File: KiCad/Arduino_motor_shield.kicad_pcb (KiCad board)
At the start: 2 copper layers, 25.9 x 59.9 mm, 19 parts, among them J1 Arduino header 1, J2 DC jack, J3 Arduino header 2, J4 Motors conn, U1 TB6612FNG

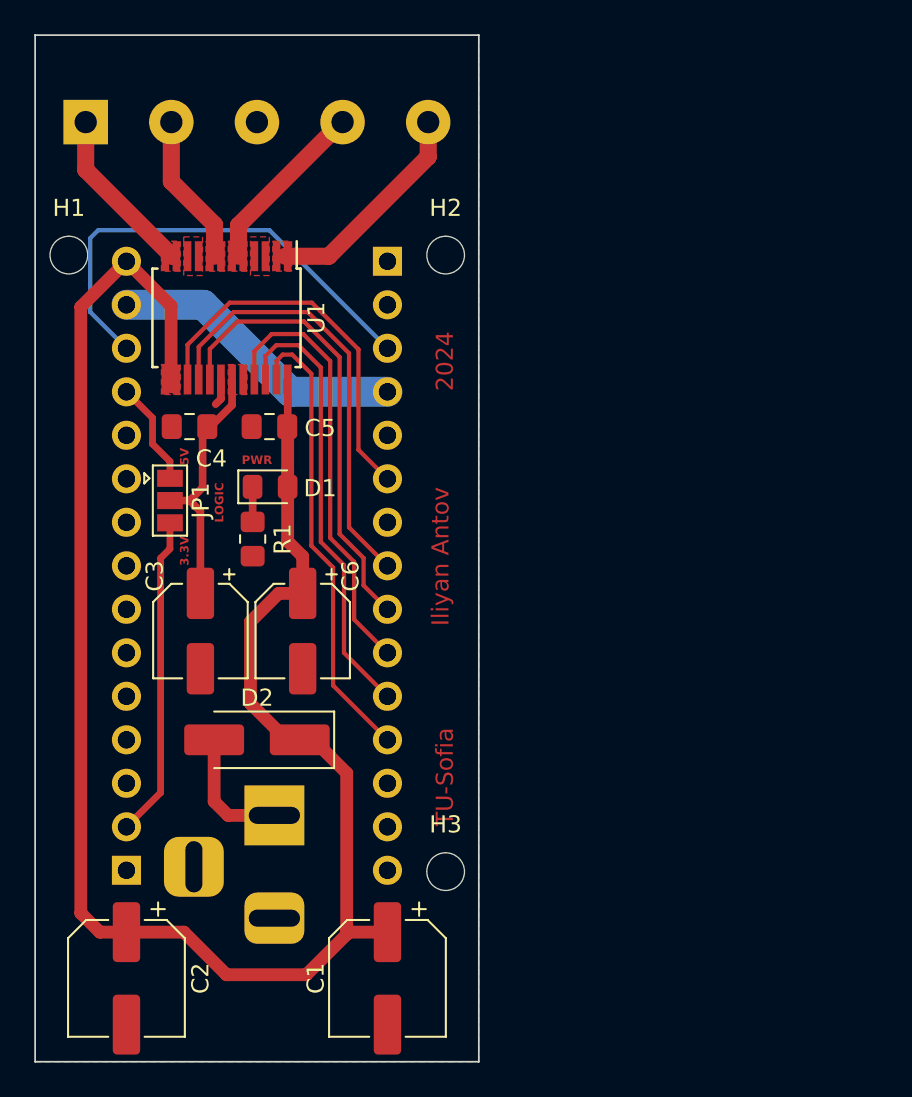
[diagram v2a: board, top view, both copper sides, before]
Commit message: Freed up a PWM pin on the Arduino
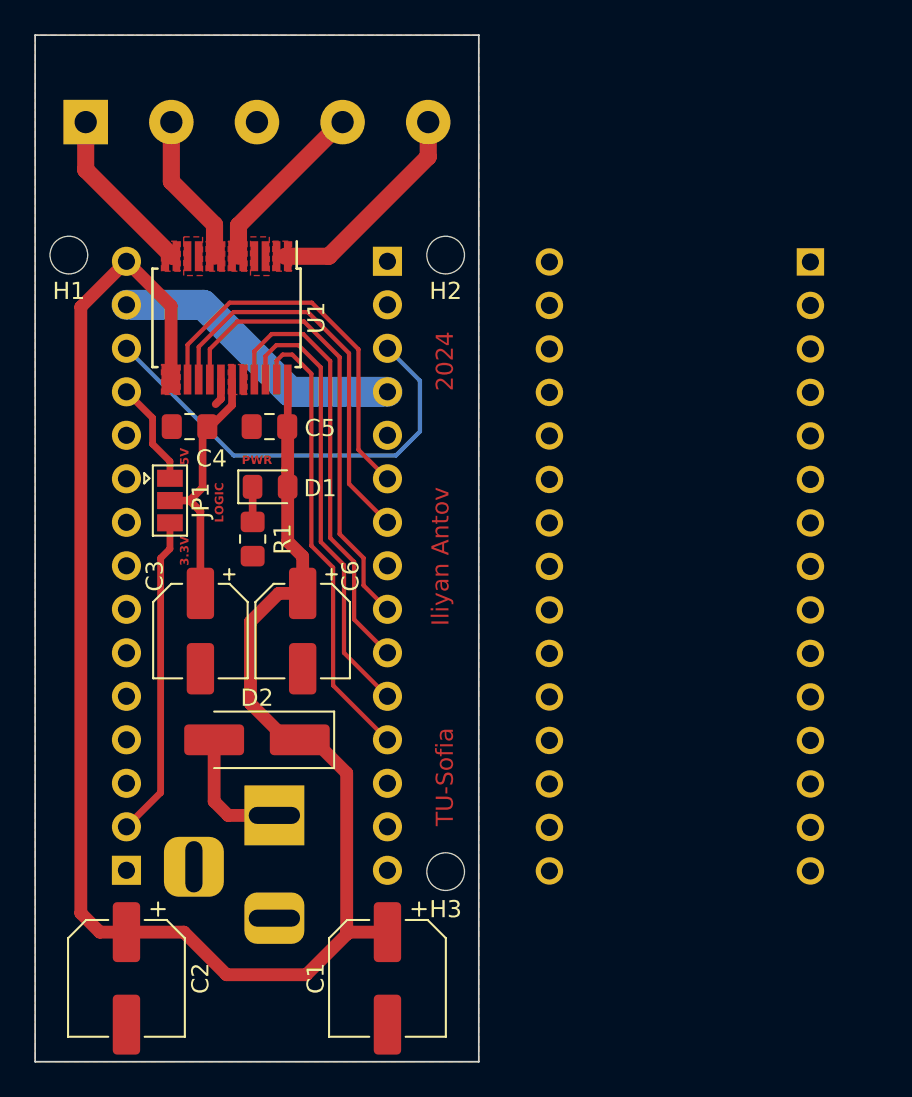
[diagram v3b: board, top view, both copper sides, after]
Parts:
- moved A1 24.7 mm to (166.3, 77.8)
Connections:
- U1 pad 16: /~D5 -> /D4
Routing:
- net /~D5: track 25.9 -> 0.00 mm
- net /D4: track 0.00 -> 23.3 mm
- net /~{RESET}: track 27.7 -> 25.9 mm
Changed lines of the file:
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@@
     (property "ki_keywords" "mounting hole")
     (attr exclude_from_pos_files)
-    (fp_text reference "H3" (at 0 -2.75) (layer "F.SilkS")
+    (fp_text reference "H3" (at 0 2.2) (layer "F.SilkS")
         (effects (font (size 1 1) (thickness 0.15)))
     )
@@
       (net 42 "/~D3") (pinfunction "PWMB") (pintype "input"))
     (pad "16" smd rect (at 3.6 1.625 270) (size 1.75 0.45) (layers "F.Cu" "F.Paste" "F.Mask")
-      (net 37 "/~D5") (pinfunction "BIN2") (pintype "input"))
+      (net 43 "/D4") (pinfunction "BIN2") (pintype "input"))
     (pad "17" smd rect (at 3.6 0.975 270) (size 1.75 0.45) (layers "F.Cu" "F.Paste" "F.Mask")
       (net 36 "/~D6") (pinfunction "BIN1") (pintype "input"))
@@
     (property "ki_keywords" "mounting hole")
     (attr exclude_from_pos_files)
-    (fp_text reference "H1" (at 0 -2.75) (layer "F.SilkS")
+    (fp_text reference "H1" (at 0 2.1) (layer "F.SilkS")
         (effects (font (size 1 1) (thickness 0.15)))
     )
@@
     (property "ki_keywords" "mounting hole")
     (attr exclude_from_pos_files)
-    (fp_text reference "H2" (at 0 -2.75) (layer "F.SilkS")
+    (fp_text reference "H2" (at 0 2.1) (layer "F.SilkS")
         (effects (font (size 1 1) (thickness 0.15)))
     )
@@
   )
   (footprint "Module:Arduino_Nano" (layer "B.Cu")
-    (at 141.60276 77.764 180)
+    (at 166.3 77.8 180)
     (descr "Arduino Nano, http://www.mouser.com/pdfdocs/Gravitech_Arduino_Nano3_0.pdf")
     (tags "Arduino Nano")
@@
   (segment (start 136.728294 81.28) (end 132.842 81.28) (width 0.25) (layer "F.Cu") (net 36))
   (segment (start 131.22976 82.89224) (end 131.22976 84.666) (width 0.25) (layer "F.Cu") (net 36))
-  (segment (start 132.614183 80.73) (end 136.956112 80.73) (width 0.25) (layer "F.Cu") (net 37))
-  (segment (start 130.57976 84.666) (end 130.57976 82.764423) (width 0.25) (layer "F.Cu") (net 37))
-  (segment (start 136.956112 80.73) (end 139.36 83.133888) (width 0.25) (layer "F.Cu") (net 37))
-  (segment (start 130.57976 82.764423) (end 132.614183 80.73) (width 0.25) (layer "F.Cu") (net 37))
-  (segment (start 139.36 93.30124) (end 141.60276 95.544) (width 0.25) (layer "F.Cu") (net 37))
-  (segment (start 139.36 83.133888) (end 139.36 93.30124) (width 0.25) (layer "F.Cu") (net 37))
   (segment (start 135.001 110.118) (end 132.30076 110.118) (width 0.75) (layer "F.Cu") (net 38))
   (segment (start 131.48276 109.3) (end 131.48276 105.704) (width 0.75) (layer "F.Cu") (net 38))
   (segment (start 132.30076 110.118) (end 131.48276 109.3) (width 0.75) (layer "F.Cu") (net 38))
-  (segment (start 134.70476 75.946) (end 141.60276 82.844) (width 0.25) (layer "B.Cu") (net 40))
-  (segment (start 126.36276 82.844) (end 124.25 80.73124) (width 0.25) (layer "B.Cu") (net 40))
-  (segment (start 124.714 75.946) (end 134.70476 75.946) (width 0.25) (layer "B.Cu") (net 40))
-  (segment (start 124.25 76.41) (end 124.714 75.946) (width 0.25) (layer "B.Cu") (net 40))
-  (segment (start 124.25 80.73124) (end 124.25 76.41) (width 0.25) (layer "B.Cu") (net 40))
+  (segment (start 126.36276 82.844) (end 132.61776 89.099) (width 0.25) (layer "B.Cu") (net 40))
+  (segment (start 132.61776 89.099) (end 142.101 89.099) (width 0.25) (layer "B.Cu") (net 40))
+  (segment (start 142.101 89.099) (end 143.5 87.7) (width 0.25) (layer "B.Cu") (net 40))
+  (segment (start 143.5 84.74124) (end 141.60276 82.844) (width 0.25) (layer "B.Cu") (net 40))
+  (segment (start 143.5 87.7) (end 143.5 84.74124) (width 0.25) (layer "B.Cu") (net 40))
   (segment (start 137.18393 80.18) (end 132.386365 80.18) (width 0.25) (layer "F.Cu") (net 42))
   (segment (start 141.60276 90.464) (end 139.91 88.77124) (width 0.25) (layer "F.Cu") (net 42))
@@
   (segment (start 139.91 88.77124) (end 139.91 82.90607) (width 0.25) (layer "F.Cu") (net 42))
   (segment (start 132.386365 80.18) (end 129.92976 82.636605) (width 0.25) (layer "F.Cu") (net 42))
+  (segment (start 130.57976 82.764423) (end 132.614183 80.73) (width 0.25) (layer "F.Cu") (net 43))
+  (segment (start 132.614183 80.73) (end 136.956112 80.73) (width 0.25) (layer "F.Cu") (net 43))
+  (segment (start 139.36 90.76124) (end 141.60276 93.004) (width 0.25) (layer "F.Cu") (net 43))
+  (segment (start 136.956112 80.73) (end 139.36 83.133888) (width 0.25) (layer "F.Cu") (net 43))
+  (segment (start 130.57976 84.666) (end 130.57976 82.764423) (width 0.25) (layer "F.Cu") (net 43))
+  (segment (start 139.36 83.133888) (end 139.36 90.76124) (width 0.25) (layer "F.Cu") (net 43))
   (segment (start 139.658 98.67924) (end 139.658 95.314993) (width 0.25) (layer "F.Cu") (net 44))
   (segment (start 134.843524 82.012) (end 133.82976 83.025764) (width 0.25) (layer "F.Cu") (net 44))
@@
       )
     )
-  )
-  (zone (net 0) (net_name "") (layer "F.Mask") (hatch edge 0.5)
-    (connect_pads (clearance 0.25))
-    (min_thickness 0.25) (filled_areas_thickness no)
-    (fill yes (thermal_gap 0.5) (thermal_bridge_width 0.5))
-    (polygon
-      (pts
-        (xy 121 64.5)
-        (xy 147 64.5)
-        (xy 147 124.5)
-        (xy 121 124.5)
-      )
-    )

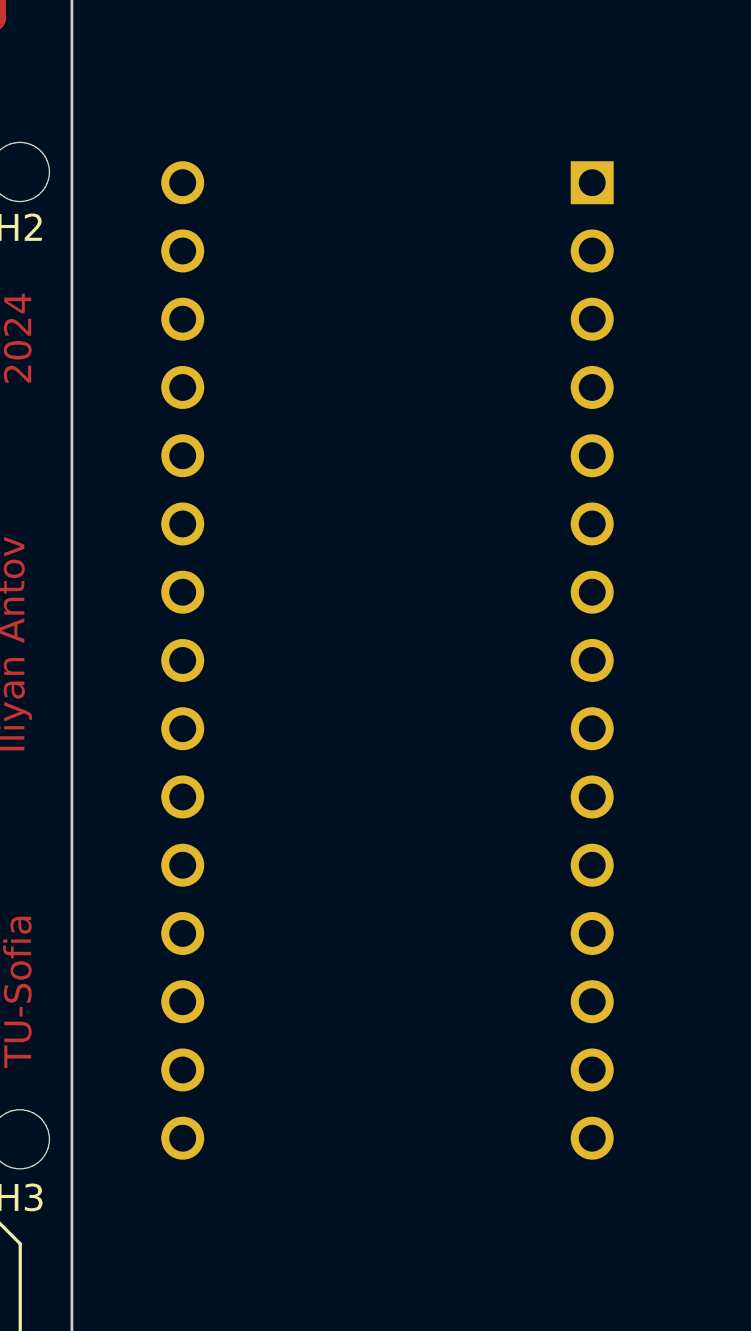
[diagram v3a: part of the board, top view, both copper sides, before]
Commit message: Added manufacture data PDF
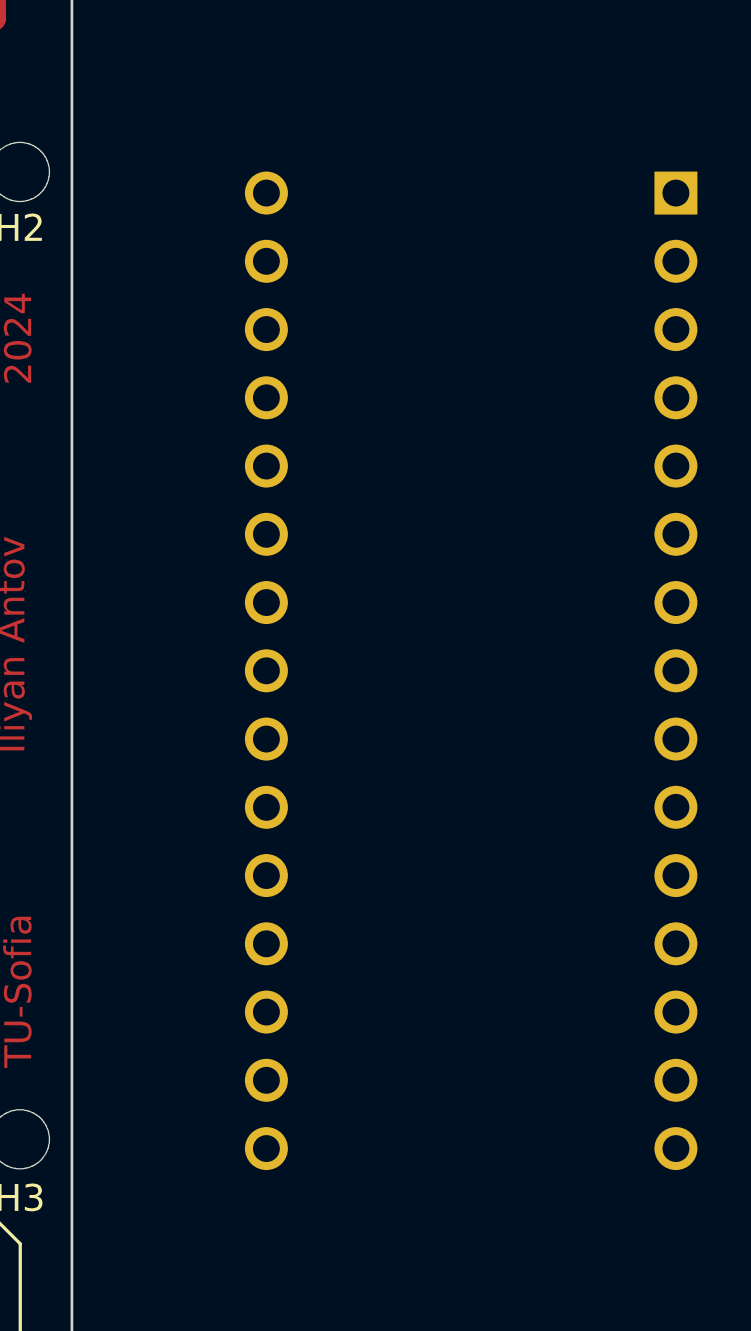
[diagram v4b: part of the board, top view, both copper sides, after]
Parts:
- moved A1 3.14 mm to (169.4, 78.2)
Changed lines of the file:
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@@
   )
   (footprint "Module:Arduino_Nano" (layer "B.Cu")
-    (at 166.3 77.8 180)
+    (at 169.415 78.185 180)
     (descr "Arduino Nano, http://www.mouser.com/pdfdocs/Gravitech_Arduino_Nano3_0.pdf")
     (tags "Arduino Nano")
@@
     )
   )
+  (zone (net 0) (net_name "") (layer "F.Cu") (hatch edge 0.5)
+    (connect_pads (clearance 0))
+    (min_thickness 0.25) (filled_areas_thickness no)
+    (keepout (tracks not_allowed) (vias not_allowed) (pads not_allowed) (copperpour not_allowed) (footprints allowed))
+    (fill (thermal_gap 0.5) (thermal_bridge_width 0.5))
+    (polygon
+      (pts
+        (xy 128.75 88.325)
+        (xy 128.74524 88.134)
+        (xy 129.276704 88.134)
+        (xy 129.275 88.325)
+      )
+    )
+  )
   (zone (net 63) (net_name "/AO2") (layer "F.Cu") (hatch edge 0.5)
     (priority 6)
@@
       )
     )
+  )
+  (zone (net 0) (net_name "") (layer "F.Cu") (hatch edge 0.5)
+    (connect_pads (clearance 0))
+    (min_thickness 0.25) (filled_areas_thickness no)
+    (keepout (tracks not_allowed) (vias not_allowed) (pads not_allowed) (copperpour not_allowed) (footprints allowed))
+    (fill (thermal_gap 0.5) (thermal_bridge_width 0.5))
+    (polygon
+      (pts
+        (xy 131.65476 83.791)
+        (xy 131.65 83.6)
+        (xy 132.106464 83.6)
+        (xy 132.10476 83.791)
+      )
+    )
